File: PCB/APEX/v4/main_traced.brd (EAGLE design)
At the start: 76.2 x 52.7 mm, 22 parts

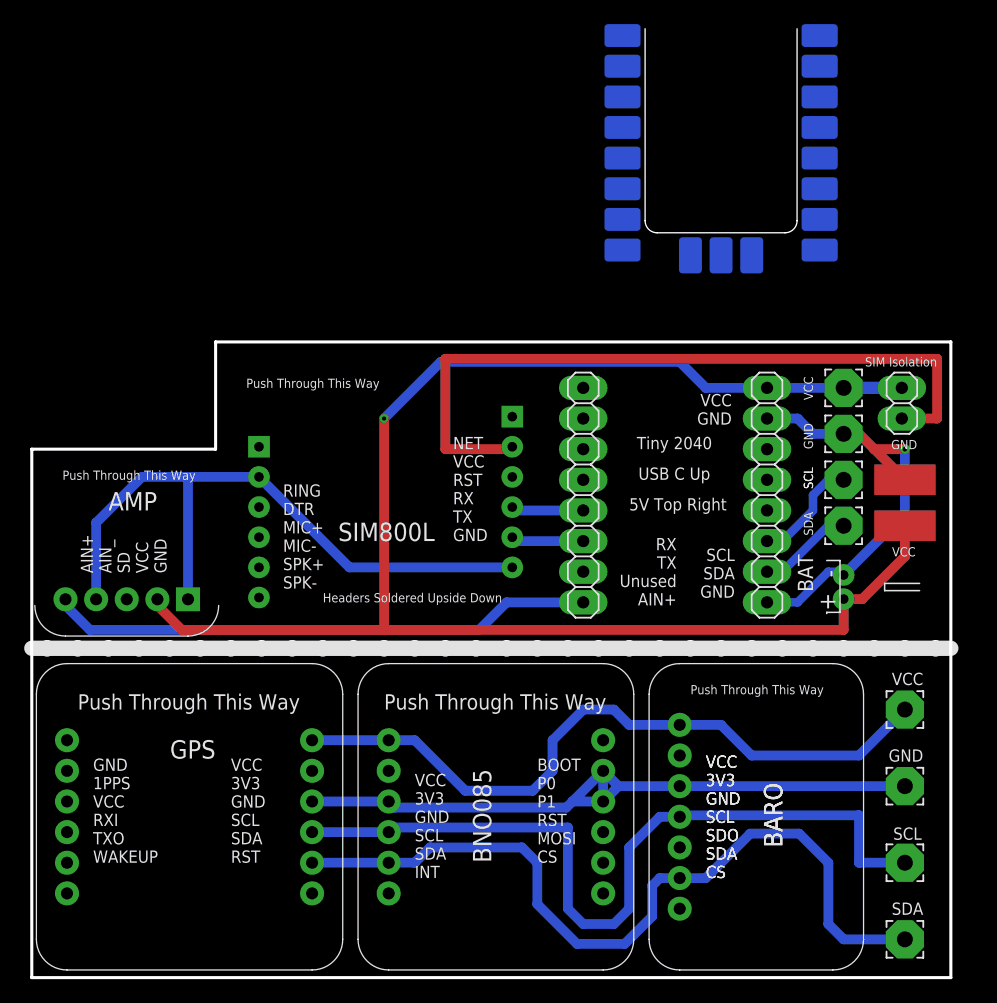
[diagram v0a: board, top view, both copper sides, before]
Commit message: implement vcc plane
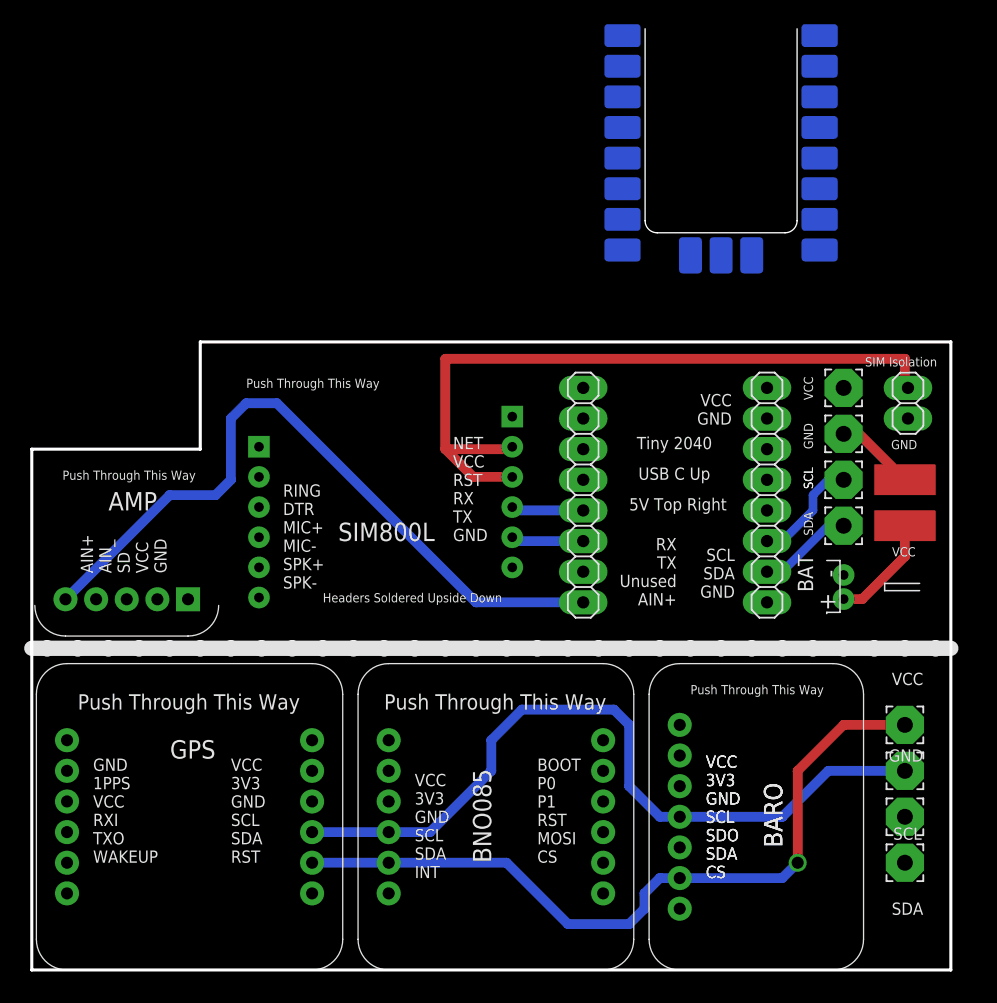
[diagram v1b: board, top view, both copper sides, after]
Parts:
- moved SENS-SDA 17.8 mm to (73.7, 40.6)
- moved SENS-VCC 12.7 mm to (73.7, 29.2)
- moved SENS-SCL 7.62 mm to (73.7, 36.8)
- moved SENS-GND 2.54 mm to (73.7, 33.0)
- moved SIMISO 0.51 mm to (73.9, 67.3), turned to 90 degrees
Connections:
- net SIMPOW: now also U$1.RST
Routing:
- net VCC: track 191.5 -> 9.09 mm, vias 1 -> 0
- net GND: track 149.9 -> 6.66 mm, vias 1 -> 0
- net AIN+: track 45.2 -> 59.5 mm
- net SCL: track 76.4 -> 72.3 mm
- net SDA: track 75.2 -> 71.2 mm, vias 0 -> 1
- net SIMPOW: track 61.8 -> 60.2 mm
- added copper zone on layer 1, net VCC
- removed copper zone on layer 1, net GND
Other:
- board size 76.2 x 52.7 mm -> 76.2 x 52.1 mm

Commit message: battery connector cutout
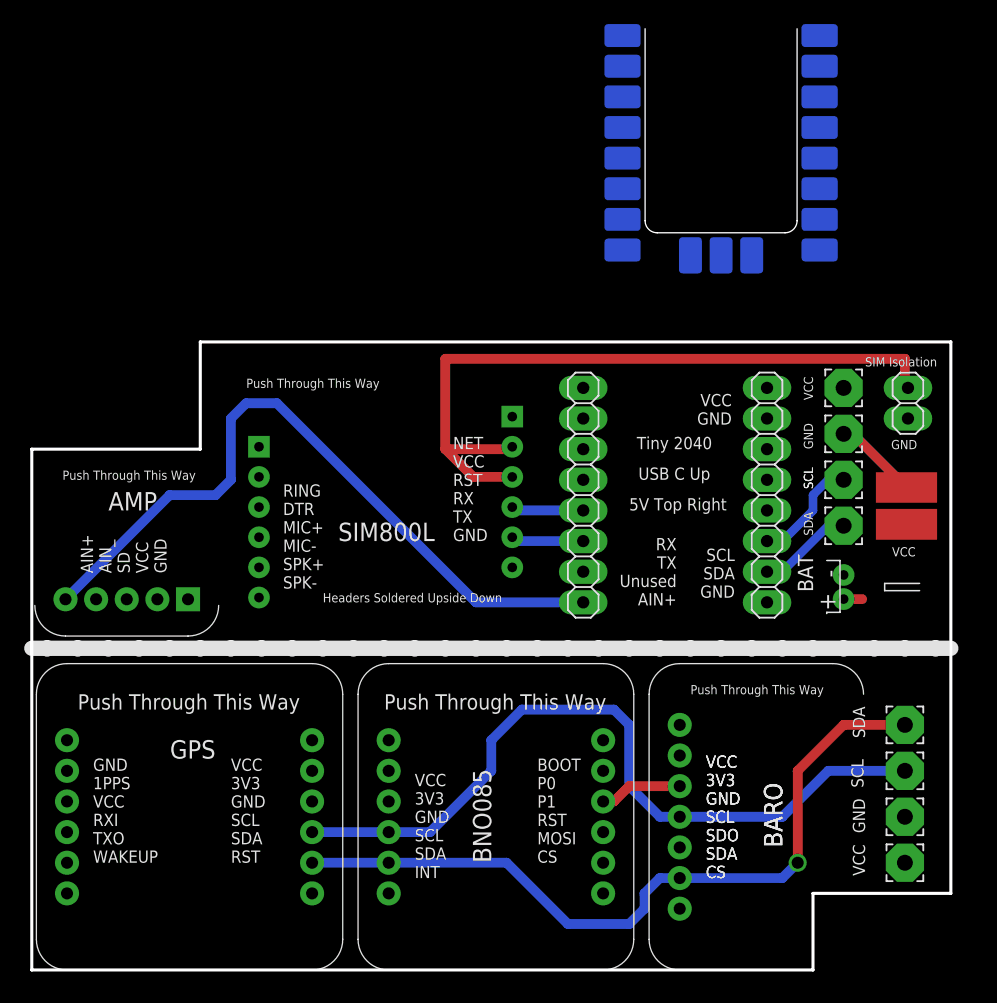
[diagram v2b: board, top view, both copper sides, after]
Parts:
- moved EXTGND 0.65 mm to (73.8, 60.3)
- moved EXTV+ 0.18 mm to (73.8, 57.3)
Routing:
- net VCC: track 9.09 -> 1.54 mm
- net GND: track 6.66 -> 13.9 mm
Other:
- outline, holes or cut-outs redrawn
